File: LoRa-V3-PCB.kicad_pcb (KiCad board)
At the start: 2 copper layers, 62 x 50 mm, 84 parts, among them IC1 114993121, IC10 BR24G1MFVT-5AE2, IC11 BR24G1MFVT-5AE2, IC12 AEM00920, IC13 MCP73123T-22SI/MF, IC2 CP2102N-Axx-xQFN24, IC3 USBLC6-2P6, IC5 BME680, IC6 SHT40-BD1B-R2, IC7 TSL25911FN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

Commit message: fix lights
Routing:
- net SWDIO: track 31.3 -> 30.0 mm
- net SWCLK: track 32.6 -> 31.5 mm

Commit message: small
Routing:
- net GND: vias 74 -> 75

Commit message: several fixes
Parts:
- SW1: footprint 1GlobalFootprintsLibrary:Wurth-4343X10458XX -> 1projectLibrary:Wurth-4343X10458XX
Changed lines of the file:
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@@
 		)
 	)
-	(footprint "1GlobalFootprintsLibrary:Wurth-4343X10458XX"
+	(footprint "1projectLibrary:Wurth-4343X10458XX"
 		(layer "F.Cu")
 		(at 115.75 107.5 90)
@@
 			)
 		)
-		(property "Footprint" "1GlobalFootprintsLibrary:Wurth-4343X10458XX"
+		(property "Footprint" "1projectLibrary:Wurth-4343X10458XX"
 			(at -0.1 0 -90)
 			(unlocked yes)
@@
 			(layer "F.Fab")
 		)
+		(fp_text user "SWITCH EDGE"
+			(at 0 -2.75 -90)
+			(layer "Dwgs.User")
+			(effects
+				(font
+					(size 0.2 0.2)
+					(thickness 0.15)
+				)
+			)
+		)
 		(fp_text user "PCB EDGE"
 			(at 0 -1.7 -90)
@@
 				(font
 					(size 0.24 0.24)
-					(thickness 0.15)
-				)
-			)
-		)
-		(fp_text user "SWITCH EDGE"
-			(at 0 -2.75 -90)
-			(layer "Dwgs.User")
-			(effects
-				(font
-					(size 0.2 0.2)
 					(thickness 0.15)
 				)
@@
 			(pintype "passive")
 		)
-		(model "C:/Users/pasca/Documents/Projects/Electronica/myComponents/1globallibraries/3dmodels/wurth-434331045822.stp"
+		(model "${KIPRJMOD}/inputs/3dmodels/wurth-434331045822.stp"
 			(offset
 				(xyz 0 0 0)

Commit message: fix SHT40 footprint
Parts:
- IC6: footprint 1GlobalFootprintsLibrary:SHT4X -> 1projectLibrary:SHT4X

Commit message: wip
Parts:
- C24: value C0603C106M8PACTU -> 47uF 10V; footprint 1projectLibrary:C_0603_nominal -> Capacitor_Tantalum_SMD:CP_EIA-3528-12_Kemet-T
- moved CONN8 0.75 mm to (163.5, 111.0)
- moved Q4 0.75 mm to (132.2, 91.5)
- moved JP1 0.50 mm to (130.8, 108.5)
- moved R4 0.50 mm to (128.0, 108.5)
- moved C1 0.25 mm to (146.8, 90.8)
- moved C10 0.25 mm to (145.2, 90.8)
- moved C5 0.25 mm to (142.2, 90.8)
- moved C6 0.25 mm to (136.2, 90.8)
- moved C7 0.25 mm to (134.8, 90.8)
- moved C8 0.25 mm to (143.8, 90.8)
- moved R10 0.25 mm to (139.2, 90.8)
- moved R8 0.25 mm to (137.8, 90.8)
- moved R9 0.25 mm to (140.8, 90.8)
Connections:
- IC12 pad 9: unconnected-(IC12-SHIP_MODE-Pad9) -> GND
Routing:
- net CHG-OUT: track 27.8 -> 30.2 mm
- net VDD-SENSORS-EEPROM: track 136.8 -> 135.9 mm
- net UART1-TX: track 19.9 -> 20.7 mm
- net VBAT: track 49.6 -> 50.4 mm
- net VDD-Display: track 37.9 -> 37.4 mm
- net +3.3V: track 81.8 -> 81.6 mm, vias 3 -> 4
- net GND: vias 75 -> 74

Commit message: wip
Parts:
- removed C21, C23: C0603C106M8PACTU, 1projectLibrary:C_0603_nominal
- removed IC12: AEM00920, 1projectLibrary:QFN-24-1EP_4x4mm_P0.5mm_EP2.15x2.15mm-epeas
- added C16: C1608X7S1A475K080AC, 1projectLibrary:C_0603_nominal, F.Cu at (130.0, 111.5)
- added C9: 100nF, 1projectLibrary:C_0603_nominal, F.Cu at (121.0, 118.2)
- added IC4: BQ25504RGTR, 1projectLibrary:VQFN-16-1EP_3x3mm_P0.5mm_EP1.6x1.6mm_ThermalVias, F.Cu at (125.8, 114.5)
- added R19: CR0603-FX-2203ELF, 1projectLibrary:R_0603_nominal, F.Cu at (121.0, 115.2)
- added R20: CR0603-FX-3742ELF, 1projectLibrary:R_0603_nominal, F.Cu at (125.5, 119.0)
- added R21: CR0603-FX-7501ELF, 1projectLibrary:R_0603_nominal, F.Cu at (124.0, 119.0)
- added R22: CR0603-FX-3301ELF, 1projectLibrary:R_0603_nominal, F.Cu at (130.0, 113.0)
- C20: value C0603C106M8PACTU -> ~
- R2: value CR0603-FX-6800ELF -> CR0603-FX-2203ELF
- moved L2 6.27 mm to (121.0, 112.5)
- moved R5 5.06 mm to (130.0, 114.5), turned to 180 degrees
- moved R2 4.03 mm to (121.0, 116.8), turned to 0 degrees
- moved R16 3.02 mm to (130.0, 116.0), turned to 180 degrees
- moved C20 2.85 mm to (118.0, 114.5), turned to -90 degrees
- moved R11 2.76 mm to (128.5, 119.0)
- moved R14 2.76 mm to (127.0, 119.0)
- moved CONN4 1.25 mm to (115.8, 114.5), turned to 180 degrees
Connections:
- C13 pad 1: +5V -> Net-(IC2-VREGIN)
- CONN1 pad A4-B9: +5V -> Net-(IC2-VREGIN)
- CONN1 pad B4-A9: +5V -> Net-(IC2-VREGIN)
- IC2 pad 7: +5V -> Net-(IC2-VREGIN)
- IC3 pad 5: +5V -> Net-(IC2-VREGIN)
- R11 pad 1: Net-(IC12-SET_OVDIS) -> GND
- R11 pad 2: Net-(IC12-SET_CHRDY) -> Net-(IC4-VBAT_UV)
- R13 pad 1: +5V -> Net-(IC2-VREGIN)
- R14 pad 1: CHG-OUT -> Net-(IC4-VBAT_UV)
- R14 pad 2: Net-(IC12-SET_OVDIS) -> Net-(IC4-VRDIV)
- R16 pad 2: Net-(IC12-CM_D) -> Net-(IC4-VRDIV)
- R2 pad 2: GND -> Solar+
- R5 pad 1: Net-(IC12-SET_CHRDY) -> Net-(IC4-OK_PROG)
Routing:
- net CHG-OUT: track 30.2 -> 13.4 mm, vias 3 -> 1
- net Solar+: track 11.5 -> 0.00 mm
- net +5V: track 55.5 -> 45.0 mm, vias 5 -> 4
- net VINT: track 10.2 -> 0.00 mm
- net Net-(IC4-LBST): track 4.99 -> 0.00 mm
- net Net-(IC12-SET_OVDIS): track 4.81 -> 0.00 mm
- net Net-(IC4-OK_HYST): track 3.99 -> 0.00 mm
- net Net-(IC4-VOC_SAMP): track 4.50 -> 0.71 mm
- net Net-(IC12-SET_CHRDY): track 3.79 -> 0.00 mm
- net Net-(IC12-CM_D): track 1.87 -> 0.00 mm
- net Net-(IC4-VREF_SAMP): track 0.00 -> 0.56 mm
- net GND: track 10.8 -> 11.4 mm, vias 74 -> 64

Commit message: finish solar power harvester
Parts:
- removed C24: 47uF 10V, Capacitor_Tantalum_SMD:CP_EIA-3528-12_Kemet-T
- removed R16: CR0603-FX-2203ELF, 1projectLibrary:R_0603_nominal
- removed R22, R4: CR0603-FX-3301ELF, 1projectLibrary:R_0603_nominal
- added C17: 100nF, 1projectLibrary:C_0603_nominal, F.Cu at (127.5, 111.5)
- added C18: C1608X7S1A475K080AC, Resistor_SMD:R_0805_2012Metric, F.Cu at (163.5, 106.0)
- added R23: CR0603-FX-2203ELF, 1projectLibrary:R_0603_nominal, F.Cu at (159.2, 113.2)
- R5: value CR0603-FX-3301ELF -> CR0603-FX-5101ELF
- moved R5 7.28 mm to (128.0, 107.5), turned to 90 degrees
- moved C16 4.00 mm to (126.0, 111.5), turned to 90 degrees
- moved C20 2.46 mm to (119.0, 112.2)
- moved R2 2.02 mm to (122.0, 115.0)
- moved R19 1.60 mm to (122.0, 116.5)
- moved IC4 1.41 mm to (126.8, 115.5)
- moved JP1 1.41 mm to (129.8, 107.5)
- moved C12 1.12 mm to (121.0, 107.5)
- moved C9 1.03 mm to (122.0, 118.0)
- moved L2 1.03 mm to (122.0, 112.2)
- moved C11 1.00 mm to (124.5, 105.0)
- moved CONN7 1.00 mm to (134.8, 114.5)
- moved F1 1.00 mm to (134.8, 119.0)
- moved IC13 1.00 mm to (124.5, 107.5)
- moved R11 0.90 mm to (129.0, 119.8)
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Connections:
- C13 pad 1: Net-(IC2-VREGIN) -> +5V
- CONN1 pad A4-B9: Net-(IC2-VREGIN) -> +5V
- CONN1 pad B4-A9: Net-(IC2-VREGIN) -> +5V
- IC1 pad 21: unconnected-(IC1-PA9-Pad21) -> Net-(IC1-PA9)
- IC2 pad 7: Net-(IC2-VREGIN) -> +5V
- IC3 pad 5: Net-(IC2-VREGIN) -> +5V
- IC4 pad 10: Net-(IC4-OK_PROG) -> GND
- IC4 pad 9: Net-(IC4-OK_HYST) -> GND
- R13 pad 1: Net-(IC2-VREGIN) -> +5V
- R5 pad 1: Net-(IC4-OK_PROG) -> GND
- R5 pad 2: Net-(IC4-OK_HYST) -> Net-(IC13-PROG)
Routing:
- net Net-(IC1-PA9): track 0.00 -> 40.7 mm, vias 0 -> 2
- net Solar+: track 0.00 -> 11.9 mm
- net CHG-OUT: track 13.4 -> 21.0 mm, vias 1 -> 2
- net Net-(IC4-VBAT_UV): track 0.00 -> 4.89 mm
- net Net-(IC4-VRDIV): track 0.00 -> 4.28 mm
- net Net-(IC4-VBAT_OV): track 0.00 -> 4.28 mm
- net Net-(IC4-VOC_SAMP): track 0.71 -> 4.84 mm
- net Net-(IC4-LBST): track 0.00 -> 4.05 mm
- net Net-(IC4-VSTOR): track 0.00 -> 3.52 mm
- net Net-(IC4-VREF_SAMP): track 0.56 -> 3.29 mm
- net +3.3V: track 81.6 -> 83.1 mm, vias 4 -> 3
- net SWDIO: track 30.0 -> 31.4 mm
- net +5V: track 45.0 -> 45.9 mm, vias 4 -> 5
- net ~{DISPLAY-RESET}: track 30.4 -> 31.2 mm
- net SPI2-SCK: track 33.0 -> 33.8 mm
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
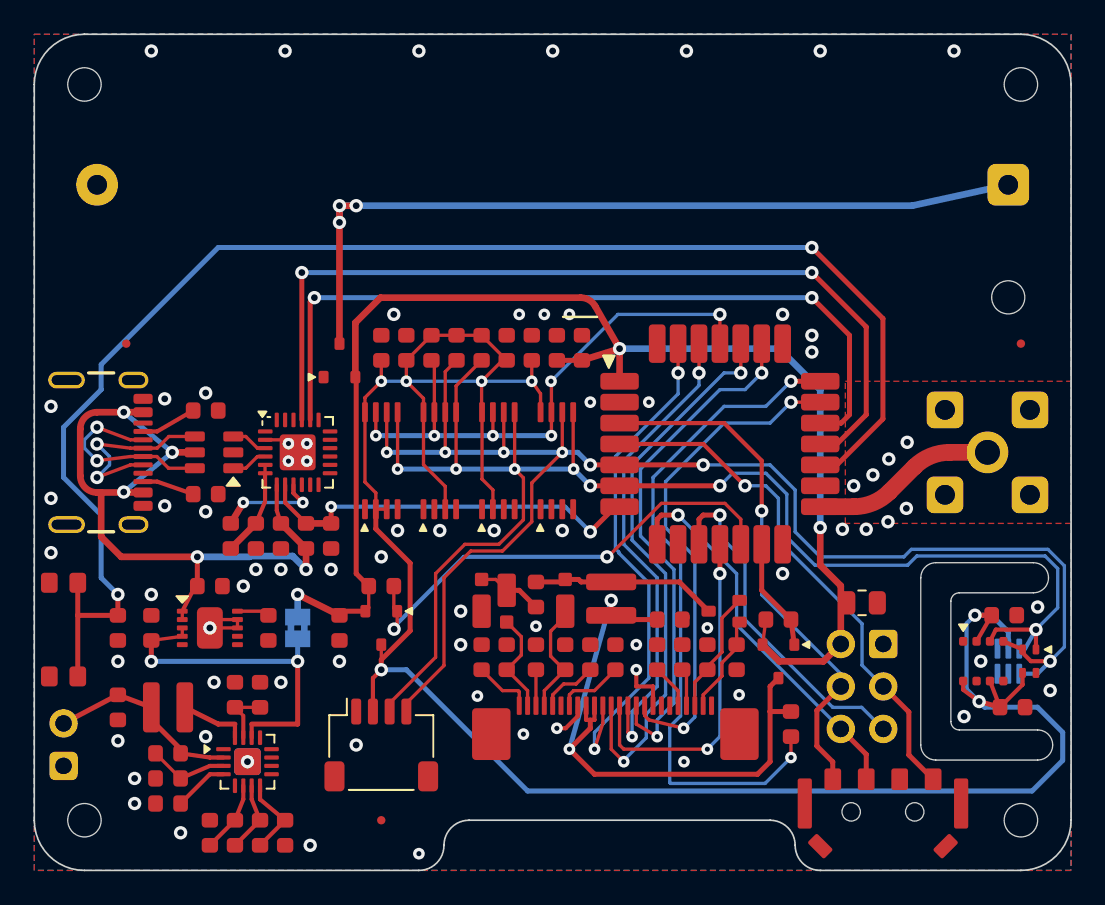
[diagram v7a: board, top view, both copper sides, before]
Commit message: improve solar layout
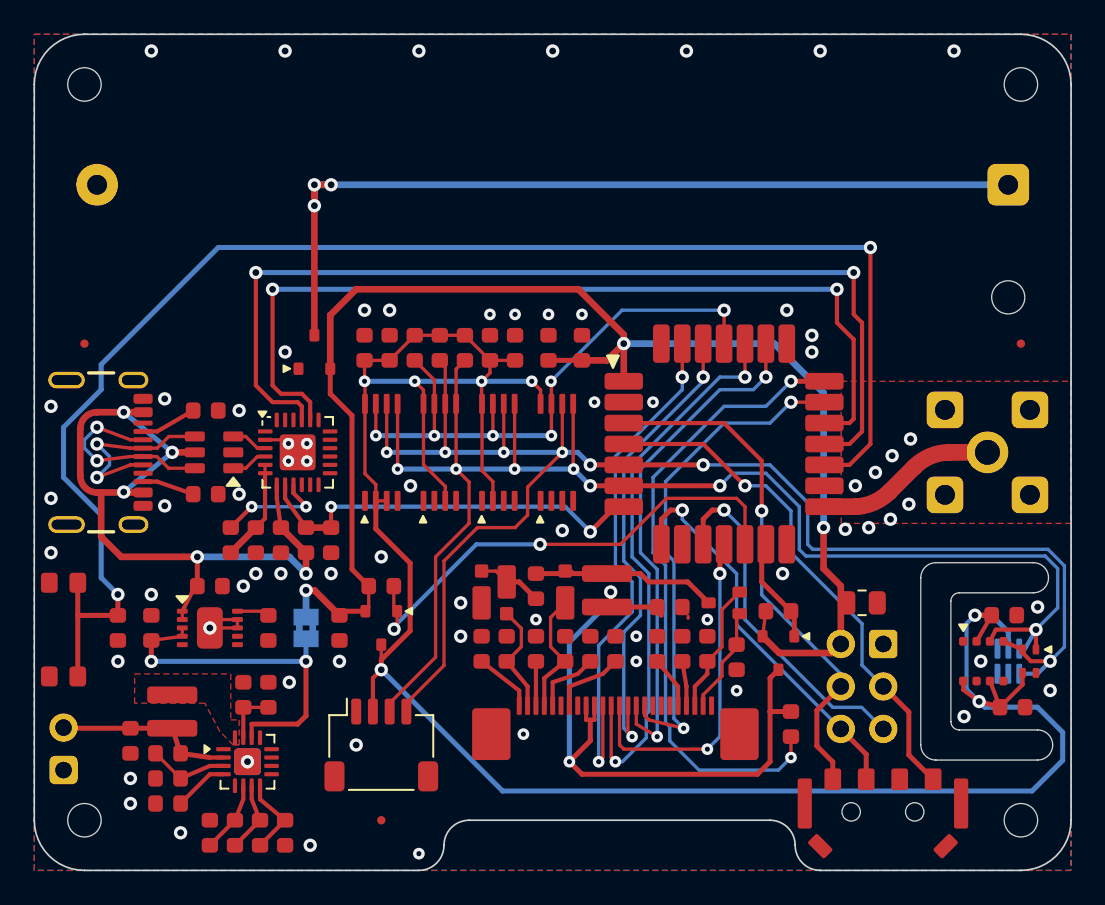
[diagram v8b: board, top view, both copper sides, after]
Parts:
- moved F2 2.50 mm to (117.0, 90.5)
- moved C20 2.14 mm to (119.8, 114.2)
- moved Q4 1.58 mm to (130.8, 91.0)
- moved C5 1.00 mm to (141.2, 90.8)
- moved C6 1.00 mm to (135.2, 90.8)
- moved C7 1.00 mm to (133.8, 90.8)
- moved C8 1.00 mm to (142.8, 90.8)
- moved R10 1.00 mm to (138.2, 90.8)
- moved R8 1.00 mm to (136.8, 90.8)
- moved R9 1.00 mm to (139.8, 90.8)
- moved C22 0.75 mm to (152.0, 106.2)
- moved L1 0.56 mm to (148.2, 105.2)
- moved C10 0.50 mm to (144.8, 90.8)
- moved C15 0.50 mm to (144.0, 105.0)
- moved C16 0.50 mm to (126.5, 111.5)
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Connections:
- net Net-(CONN6-Pin_18) renamed VDD
- net Net-(IC1-PA9) renamed VDD-Display-Charge
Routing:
- net UART2-RX: track 52.6 -> 59.1 mm
- net UART2-TX: track 46.5 -> 53.0 mm
- net GND: track 10.7 -> 5.33 mm, vias 75 -> 70
- net Net-(IC4-LBST): track 4.05 -> 0.00 mm
- net +3.3V: track 83.1 -> 87.1 mm
- net VDD-Display: track 37.2 -> 40.6 mm
- net VDD-Display-Charge: track 40.7 -> 38.1 mm
- net VBAT: track 50.4 -> 52.7 mm
- net ~{WRITE-PROTECT}: track 34.6 -> 36.7 mm
- net ~{MCU-RESET}: track 88.5 -> 90.4 mm
- net I2C2-SDA: track 93.1 -> 91.3 mm
- net I2C2-SCL: track 91.7 -> 92.9 mm
- net Solar+: track 11.9 -> 10.7 mm
- net VDD-SENSORS-EEPROM: track 136.0 -> 134.9 mm
- net ~{Enable-3.3V-Switched-1}: track 28.6 -> 29.5 mm
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- added copper zone on F.Cu, net Net-(IC4-LBST)
